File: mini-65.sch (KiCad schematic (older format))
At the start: 167 parts, among them J1 AVR-ISP-6, SW1 SW_Push, U1 ATmega32U4-AU, Y1 Crystal_GND24_Small

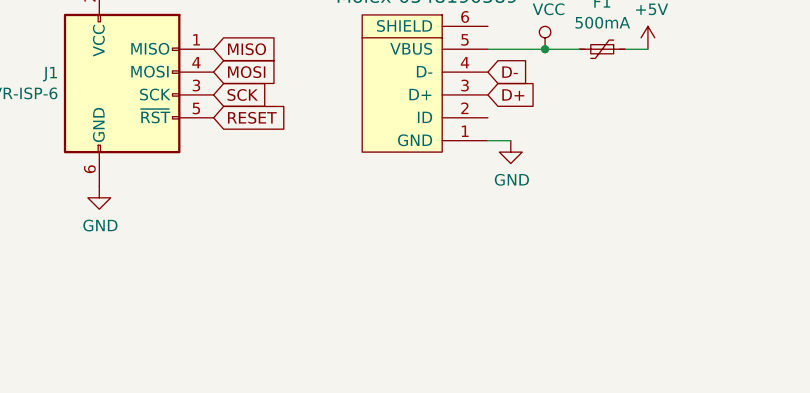
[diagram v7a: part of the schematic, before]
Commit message: Added some libraries, to try to add JST connector
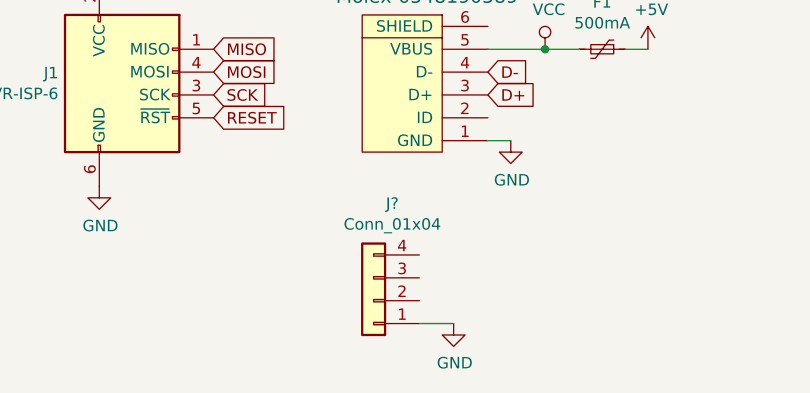
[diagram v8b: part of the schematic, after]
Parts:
- added J?: Conn_01x04, symbol Connector_Generic:Conn_01x04
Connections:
- net GND: now also J?.1 (Pin_1)
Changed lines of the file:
@@
 	1750 1200 1800 1200
-$Comp
-L power:GND #PWR0106
-U 1 1 5F19B973
-P 1200 1100
-F 0 "#PWR0106" H 1200 850 50  0001 C CNN
-F 1 "GND" H 1205 927 50  0000 C CNN
-F 2 "" H 1200 1100 50  0001 C CNN
-F 3 "" H 1200 1100 50  0001 C CNN
-	1    1200 1100
-	1    0    0    -1
-$EndComp
 $Comp
 L Switch:SW_Push SW1
@@
 Wire Wire Line
 	1850 1350 1750 1350
-Wire Wire Line
-	1150 1850 1150 1650
-Connection ~ 600  1950
-Wire Wire Line
-	600  1950 950  1950
-Wire Wire Line
-	600  1800 600  1950
-Connection ~ 600  1800
-Wire Wire Line
-	600  1450 600  1800
-Connection ~ 1050 1550
-Wire Wire Line
-	800  1550 1050 1550
-Wire Wire Line
-	800  1450 800  1550
-Connection ~ 1050 1750
-Wire Wire Line
-	800  1750 1050 1750
-Wire Wire Line
-	800  1800 800  1750
-$Comp
-L power:GND #PWR0113
-U 1 1 5F19652E
-P 600 1950
-F 0 "#PWR0113" H 600 1700 50  0001 C CNN
-F 1 "GND" H 605 1777 50  0000 C CNN
-F 2 "" H 600 1950 50  0001 C CNN
-F 3 "" H 600 1950 50  0001 C CNN
-	1    600  1950
-	1    0    0    -1
-$EndComp
-$Comp
-L Device:C_Small C2
-U 1 1 5F194FE3
-P 700 1800
-F 0 "C2" V 471 1800 50  0000 C CNN
-F 1 "22pF" V 562 1800 50  0000 C CNN
-F 2 "Capacitor_SMD:C_0805_2012Metric" H 700 1800 50  0001 C CNN
-F 3 "~" H 700 1800 50  0001 C CNN
-	1    700  1800
-	0    1    1    0
-$EndComp
-$Comp
-L Device:C_Small C1
-U 1 1 5F1942FA
-P 700 1450
-F 0 "C1" V 471 1450 50  0000 C CNN
-F 1 "22pF" V 562 1450 50  0000 C CNN
-F 2 "Capacitor_SMD:C_0805_2012Metric" H 700 1450 50  0001 C CNN
-F 3 "~" H 700 1450 50  0001 C CNN
-	1    700  1450
-	0    1    1    0
-$EndComp
-$Comp
-L Device:Crystal_GND24_Small Y1
-U 1 1 5F18D205
-P 1050 1650
-F 0 "Y1" V 1000 1800 50  0000 L CNN
-F 1 "Crystal_GND24_Small" V 1194 1605 50  0001 L CNN
-F 2 "Crystal:Crystal_SMD_3225-4Pin_3.2x2.5mm" H 1050 1650 50  0001 C CNN
-F 3 "~" H 1050 1650 50  0001 C CNN
-	1    1050 1650
-	0    1    1    0
-$EndComp
-Wire Wire Line
-	950  1650 950  1850
-Wire Wire Line
-	1150 1850 950  1850
-Connection ~ 950  1850
-Wire Wire Line
-	950  1850 950  1950
-Wire Wire Line
-	1050 1750 1950 1750
-Wire Wire Line
-	1050 1550 1950 1550
 Text GLabel 3150 1450 2    50   Input ~ 0
 SCK
@@
 Wire Wire Line
 	12050 3000 13700 3000
+Wire Wire Line
+	1050 1550 1950 1550
+Wire Wire Line
+	1050 1750 1950 1750
+Wire Wire Line
+	950  1850 950  1950
+Connection ~ 950  1850
+Wire Wire Line
+	1150 1850 950  1850
+Wire Wire Line
+	950  1650 950  1850
+$Comp
+L Device:Crystal_GND24_Small Y1
+U 1 1 5F18D205
+P 1050 1650
+F 0 "Y1" V 1000 1800 50  0000 L CNN
+F 1 "Crystal_GND24_Small" V 1194 1605 50  0001 L CNN
+F 2 "Crystal:Crystal_SMD_3225-4Pin_3.2x2.5mm" H 1050 1650 50  0001 C CNN
+F 3 "~" H 1050 1650 50  0001 C CNN
+	1    1050 1650
+	0    1    1    0
+$EndComp
+$Comp
+L Device:C_Small C1
+U 1 1 5F1942FA
+P 700 1450
+F 0 "C1" V 471 1450 50  0000 C CNN
+F 1 "22pF" V 562 1450 50  0000 C CNN
+F 2 "Capacitor_SMD:C_0805_2012Metric" H 700 1450 50  0001 C CNN
+F 3 "~" H 700 1450 50  0001 C CNN
+	1    700  1450
+	0    1    1    0
+$EndComp
+$Comp
+L Device:C_Small C2
+U 1 1 5F194FE3
+P 700 1800
+F 0 "C2" V 471 1800 50  0000 C CNN
+F 1 "22pF" V 562 1800 50  0000 C CNN
+F 2 "Capacitor_SMD:C_0805_2012Metric" H 700 1800 50  0001 C CNN
+F 3 "~" H 700 1800 50  0001 C CNN
+	1    700  1800
+	0    1    1    0
+$EndComp
+$Comp
+L power:GND #PWR0113
+U 1 1 5F19652E
+P 600 1950
+F 0 "#PWR0113" H 600 1700 50  0001 C CNN
+F 1 "GND" H 605 1777 50  0000 C CNN
+F 2 "" H 600 1950 50  0001 C CNN
+F 3 "" H 600 1950 50  0001 C CNN
+	1    600  1950
+	1    0    0    -1
+$EndComp
+Wire Wire Line
+	800  1800 800  1750
+Wire Wire Line
+	800  1750 1050 1750
+Connection ~ 1050 1750
+Wire Wire Line
+	800  1450 800  1550
+Wire Wire Line
+	800  1550 1050 1550
+Connection ~ 1050 1550
+Wire Wire Line
+	600  1450 600  1800
+Connection ~ 600  1800
+Wire Wire Line
+	600  1800 600  1950
+Wire Wire Line
+	600  1950 950  1950
+Connection ~ 600  1950
+Wire Wire Line
+	1150 1850 1150 1650
+$Comp
+L power:GND #PWR0106
+U 1 1 5F19B973
+P 1200 1100
+F 0 "#PWR0106" H 1200 850 50  0001 C CNN
+F 1 "GND" H 1205 927 50  0000 C CNN
+F 2 "" H 1200 1100 50  0001 C CNN
+F 3 "" H 1200 1100 50  0001 C CNN
+	1    1200 1100
+	1    0    0    -1
+$EndComp
+$Comp
+L Connector_Generic:Conn_01x04 J?
+U 1 1 5F8BE1D6
+P 2300 7400
+F 0 "J?" H 2218 6975 50  0000 C CNN
+F 1 "Conn_01x04" H 2218 7066 50  0000 C CNN
+F 2 "" H 2300 7400 50  0001 C CNN
+F 3 "~" H 2300 7400 50  0001 C CNN
+	1    2300 7400
+	-1   0    0    1
+$EndComp
+$Comp
+L power:GND #PWR?
+U 1 1 5F8C838A
+P 2650 7500
+F 0 "#PWR?" H 2650 7250 50  0001 C CNN
+F 1 "GND" H 2655 7327 50  0000 C CNN
+F 2 "" H 2650 7500 50  0001 C CNN
+F 3 "" H 2650 7500 50  0001 C CNN
+	1    2650 7500
+	1    0    0    -1
+$EndComp
+Wire Wire Line
+	2500 7500 2650 7500
 $EndSCHEMATC
